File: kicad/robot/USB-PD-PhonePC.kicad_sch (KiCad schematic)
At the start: 40 parts, among them IC1 TPS61253AYFFR, U11 MAX77958EWV+T, U15 ESD122DMYR

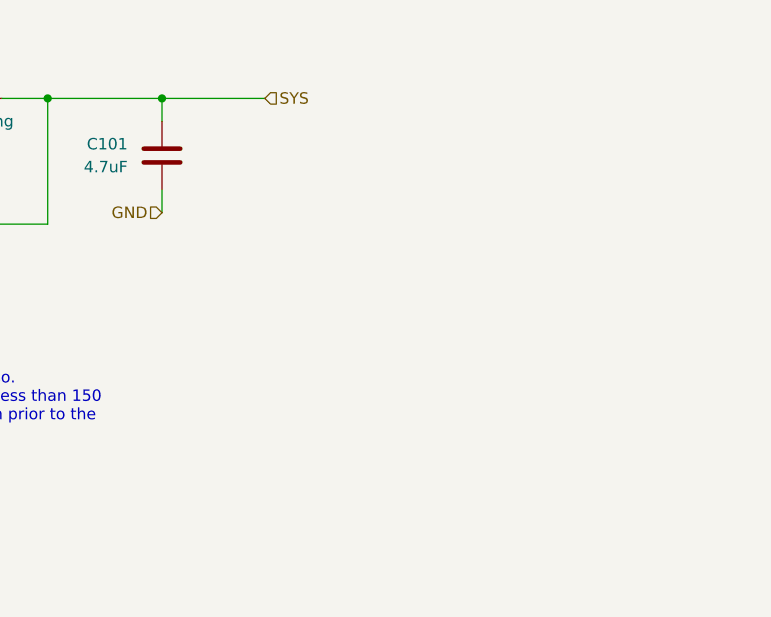
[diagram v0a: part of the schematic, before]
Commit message: Added dual mosfet to MCU PD side as well. To discuss
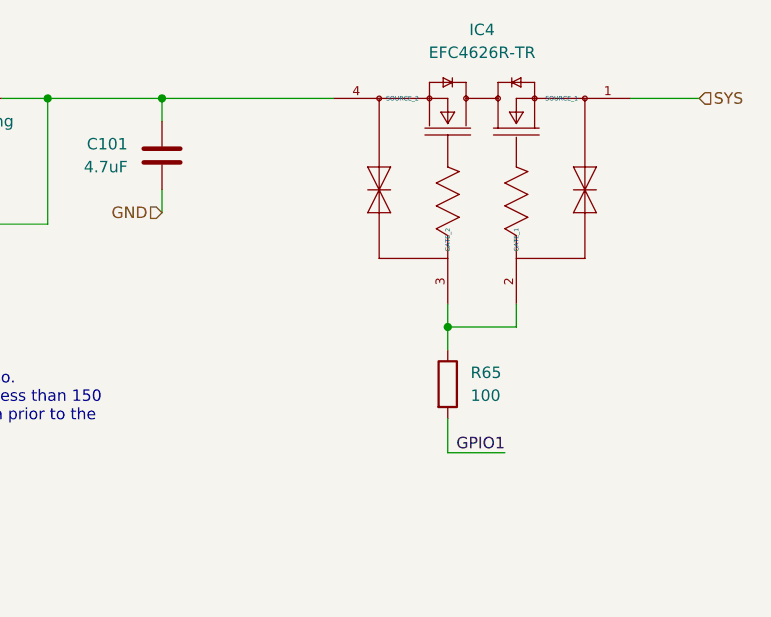
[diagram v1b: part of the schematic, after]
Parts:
- added IC4: EFC4626R-TR, Package_BGA:ON_SEMI_EFCP1010-4DG-020, symbol Power_Management:EFC4626R-TR
- added R65: 100, Resistor_SMD:R_0603_1608Metric, symbol Device:R
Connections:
- net GPIO1: now also R65.2
- net SYS: now also IC4.1 (SOURCE_1); no longer C101.1, IC1.A3 (VIN), L4.1
- new net: IC4.2 (GATE_1), IC4.3 (GATE_2), R65.1
- new net: C101.1, IC1.A3 (VIN), IC4.4 (SOURCE_2), L4.1
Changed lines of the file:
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@@
   (junction (at 231.14 267.97) (diameter 0) (color 0 0 0 0)
   )
+  (junction (at 317.5 220.98) (diameter 0) (color 0 0 0 0)
+  )
+  (junction (at 213.36 175.26) (diameter 0) (color 0 0 0 0)
+  )
   (junction (at 422.91 130.81) (diameter 0) (color 0 0 0 0)
   )
-  (junction (at 317.5 220.98) (diameter 0) (color 0 0 0 0)
-  )
-  (junction (at 213.36 175.26) (diameter 0) (color 0 0 0 0)
-  )
   (junction (at 248.92 130.81) (diameter 0) (color 0 0 0 0)
   )
@@
   )
   (junction (at 331.47 246.38) (diameter 0) (color 0 0 0 0)
+  )
+  (junction (at 454.66 156.21) (diameter 0) (color 0 0 0 0)
   )
   (junction (at 339.09 234.95) (diameter 0) (color 0 0 0 0)
@@
     (stroke (width 0) (type default) (color 0 0 0 0))
   )
+  (wire (pts (xy 454.66 166.37) (xy 454.66 170.18))
+    (stroke (width 0) (type default) (color 0 0 0 0))
+  )
   (wire (pts (xy 410.21 130.81) (xy 422.91 130.81))
     (stroke (width 0) (type default) (color 0 0 0 0))
@@
     (stroke (width 0) (type default) (color 0 0 0 0))
   )
+  (wire (pts (xy 454.66 170.18) (xy 461.01 170.18))
+    (stroke (width 0) (type default) (color 0 0 0 0))
+  )
   (wire (pts (xy 321.31 203.2) (xy 321.31 191.77))
     (stroke (width 0) (type default) (color 0 0 0 0))
@@
     (stroke (width 0) (type default) (color 0 0 0 0))
   )
+  (wire (pts (xy 462.28 153.67) (xy 462.28 156.21))
+    (stroke (width 0) (type default) (color 0 0 0 0))
+  )
   (wire (pts (xy 227.33 215.9) (xy 264.16 215.9))
     (stroke (width 0) (type default) (color 0 0 0 0))
@@
     (stroke (width 0) (type default) (color 0 0 0 0))
   )
+  (wire (pts (xy 454.66 156.21) (xy 454.66 153.67))
+    (stroke (width 0) (type default) (color 0 0 0 0))
+  )
   (wire (pts (xy 309.88 259.08) (xy 316.23 259.08))
     (stroke (width 0) (type default) (color 0 0 0 0))
@@
     (stroke (width 0) (type default) (color 0 0 0 0))
   )
+  (wire (pts (xy 422.91 130.81) (xy 441.96 130.81))
+    (stroke (width 0) (type default) (color 0 0 0 0))
+  )
   (wire (pts (xy 248.92 198.12) (xy 248.92 130.81))
     (stroke (width 0) (type default) (color 0 0 0 0))
@@
     (stroke (width 0) (type default) (color 0 0 0 0))
   )
+  (wire (pts (xy 454.66 158.75) (xy 454.66 156.21))
+    (stroke (width 0) (type default) (color 0 0 0 0))
+  )
   (wire (pts (xy 339.09 269.24) (xy 339.09 264.16))
     (stroke (width 0) (type default) (color 0 0 0 0))
@@
     (stroke (width 0) (type default) (color 0 0 0 0))
   )
+  (wire (pts (xy 462.28 156.21) (xy 454.66 156.21))
+    (stroke (width 0) (type default) (color 0 0 0 0))
+  )
+  (wire (pts (xy 474.98 130.81) (xy 482.6 130.81))
+    (stroke (width 0) (type default) (color 0 0 0 0))
+  )
   (wire (pts (xy 309.88 218.44) (xy 317.5 218.44))
     (stroke (width 0) (type default) (color 0 0 0 0))
@@
   )
   (wire (pts (xy 335.28 142.24) (xy 335.28 144.78))
-    (stroke (width 0) (type default) (color 0 0 0 0))
-  )
-  (wire (pts (xy 422.91 130.81) (xy 434.34 130.81))
     (stroke (width 0) (type default) (color 0 0 0 0))
   )
@@
     (effects (font (size 1.27 1.27)) (justify right bottom))
   )
+  (label "GPIO1" (at 461.01 170.18 180)
+    (effects (font (size 1.27 1.27)) (justify right bottom))
+  )
   (label "GPIO0" (at 330.2 280.67 0)
     (effects (font (size 1.27 1.27)) (justify left bottom))
@@
     (effects (font (size 1.27 1.27)) (justify left))
   )
-  (hierarchical_label "SYS" (shape input) (at 434.34 130.81 0)
+  (hierarchical_label "SYS" (shape input) (at 482.6 130.81 0)
     (effects (font (size 1.27 1.27)) (justify left))
   )
@@
     (pin "1")
     (pin "2")
+  )
+  (symbol (lib_id "Power_Management:EFC4626R-TR") (at 458.47 140.97 90) (unit 1)
+    (in_bom yes) (on_board yes) (fields_autoplaced)
+    (property "Reference" "IC4" (id 0) (at 458.47 123.19 90))
+    (property "Value" "EFC4626R-TR" (id 1) (at 458.47 125.73 90))
+    (property "Footprint" "Package_BGA:ON_SEMI_EFCP1010-4DG-020" (id 2) (at 415.925 150.495 0)
+      (effects (font (size 1.27 1.27)) (justify left) hide)
+    )
+    (property "Datasheet" "http://www.onsemi.com/pub/Collateral/ENA2292-D.PDF" (id 3) (at 418.465 150.495 0)
+      (effects (font (size 1.27 1.27)) (justify left) hide)
+    )
+    (property "Description" "MOSFET NCH+NCH 2.5V DRIVE" (id 4) (at 421.005 150.495 0)
+      (effects (font (size 1.27 1.27)) (justify left) hide)
+    )
+    (property "Height" "0.22" (id 5) (at 423.545 150.495 0)
+      (effects (font (size 1.27 1.27)) (justify left) hide)
+    )
+    (property "Manufacturer_Name" "onsemi" (id 6) (at 426.085 150.495 0)
+      (effects (font (size 1.27 1.27)) (justify left) hide)
+    )
+    (property "Manufacturer_Part_Number" "EFC4626R-TR" (id 7) (at 428.625 150.495 0)
+      (effects (font (size 1.27 1.27)) (justify left) hide)
+    )
+    (property "Mouser Part Number" "863-EFC4626R-TR" (id 8) (at 431.165 150.495 0)
+      (effects (font (size 1.27 1.27)) (justify left) hide)
+    )
+    (property "Mouser Price/Stock" "https://www.mouser.com/Search/Refine.aspx?Keyword=863-EFC4626R-TR" (id 9) (at 433.705 150.495 0)
+      (effects (font (size 1.27 1.27)) (justify left) hide)
+    )
+    (property "Arrow Part Number" "" (id 10) (at 436.245 150.495 0)
+      (effects (font (size 1.27 1.27)) (justify left) hide)
+    )
+    (property "Arrow Price/Stock" "" (id 11) (at 438.785 150.495 0)
+      (effects (font (size 1.27 1.27)) (justify left) hide)
+    )
+    (property "Mouser Testing Part Number" "" (id 12) (at 441.325 150.495 0)
+      (effects (font (size 1.27 1.27)) (justify left) hide)
+    )
+    (property "Mouser Testing Price/Stock" "" (id 13) (at 483.87 109.22 0)
+      (effects (font (size 1.27 1.27)) (justify left) hide)
+    )
+    (pin "1")
+    (pin "2")
+    (pin "3")
+    (pin "4")
   )
   (symbol (lib_id "Device:C") (at 231.14 259.08 0) (unit 1)
@@
       (effects (font (size 1.27 1.27)) hide)
     )
+    (pin "1")
+    (pin "2")
+  )
+  (symbol (lib_id "Device:R") (at 454.66 162.56 0) (unit 1)
+    (in_bom yes) (on_board yes) (fields_autoplaced)
+    (property "Reference" "R65" (id 0) (at 457.2 161.2899 0)
+      (effects (font (size 1.27 1.27)) (justify left))
+    )
+    (property "Value" "100" (id 1) (at 457.2 163.8299 0)
+      (effects (font (size 1.27 1.27)) (justify left))
+    )
+    (property "Footprint" "Resistor_SMD:R_0603_1608Metric" (id 2) (at 452.882 162.56 90)
+      (effects (font (size 1.27 1.27)) hide)
+    )
+    (property "Datasheet" "~" (id 3) (at 454.66 162.56 0)
+      (effects (font (size 1.27 1.27)) hide)
+    )

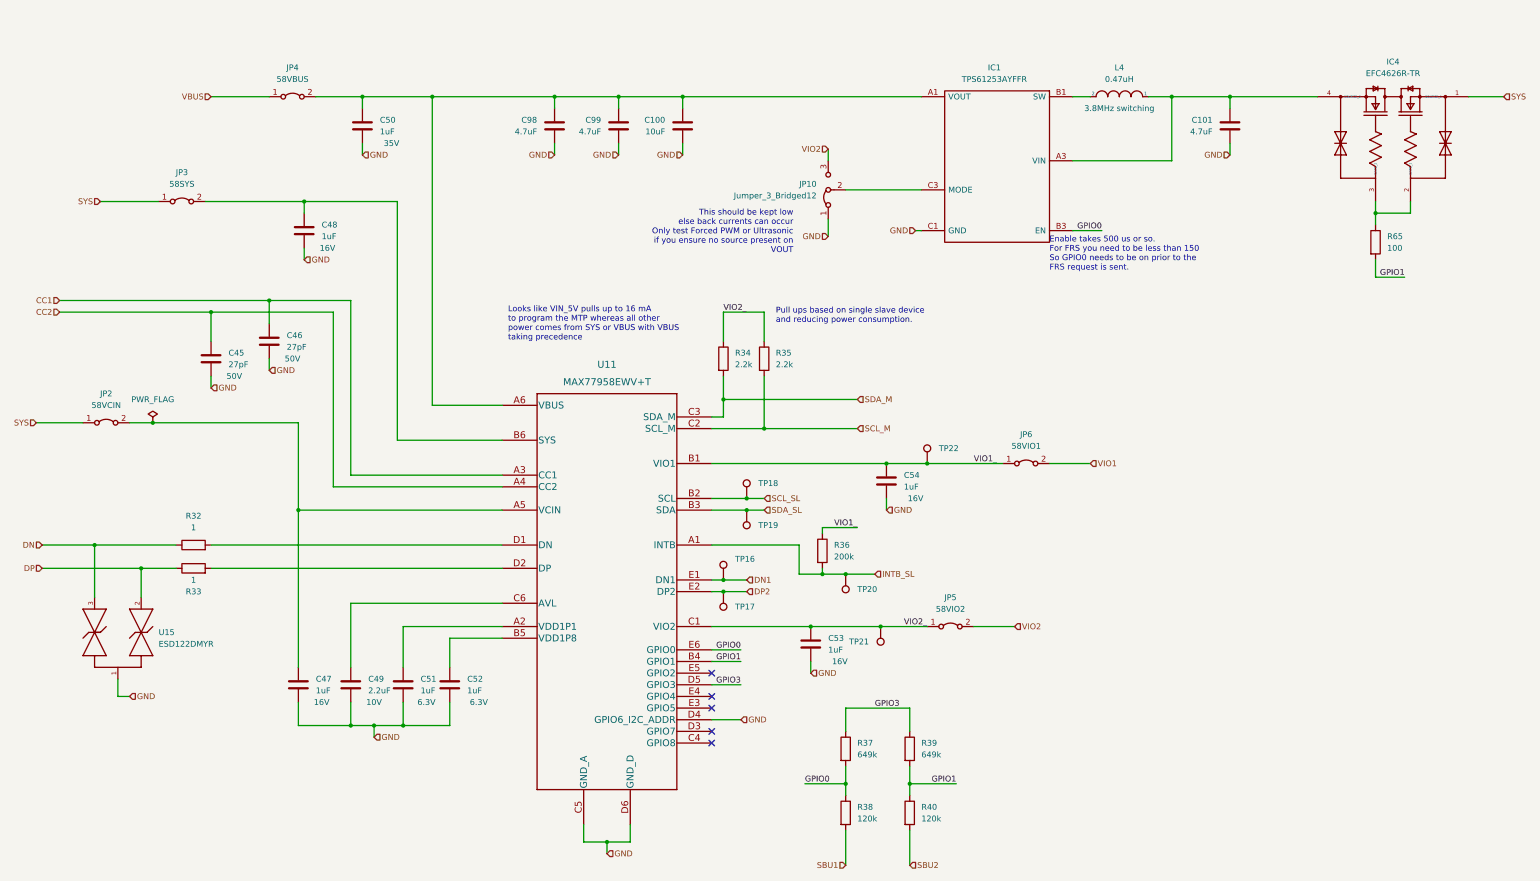
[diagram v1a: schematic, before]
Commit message: Cosmetic rework of USB-PD-PhonePC
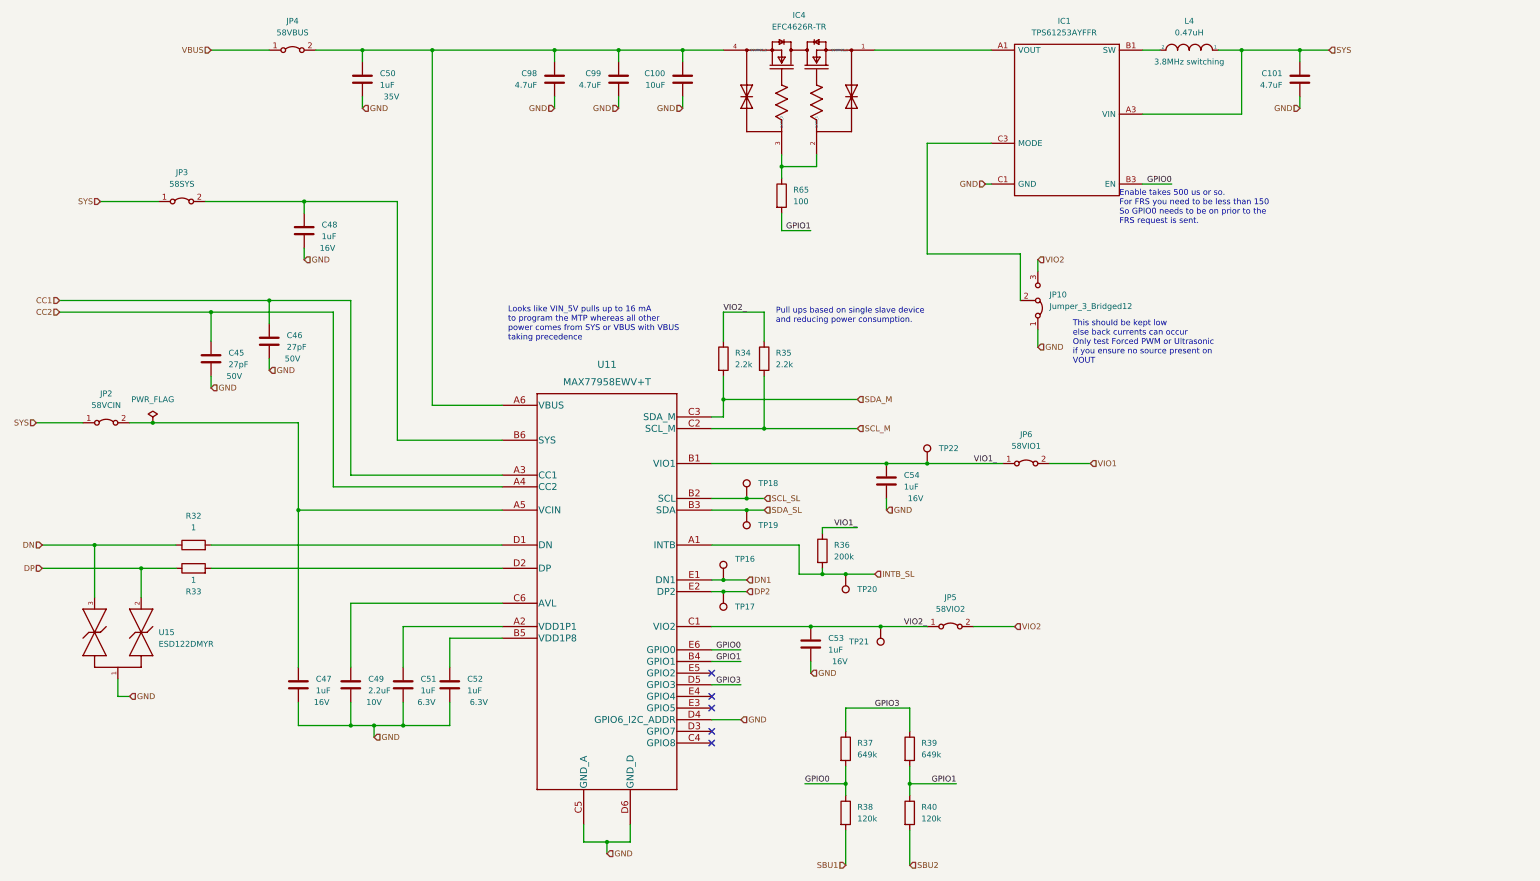
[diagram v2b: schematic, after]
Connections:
- net SYS: now also C101.1, IC1.A3 (VIN), L4.1; no longer IC4.1 (SOURCE_1)
- net at C100.1, C50.1, C98.1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: now also IC4.4 (SOURCE_2); no longer IC1.A1 (VOUT), IC1.A2 (VOUT)
- new net: IC1.A1 (VOUT), IC1.A2 (VOUT), IC4.1 (SOURCE_1)
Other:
- moved on the sheet: C100, C101, C50, C98, C99, IC1, IC4, JP10, JP4, L4, R65

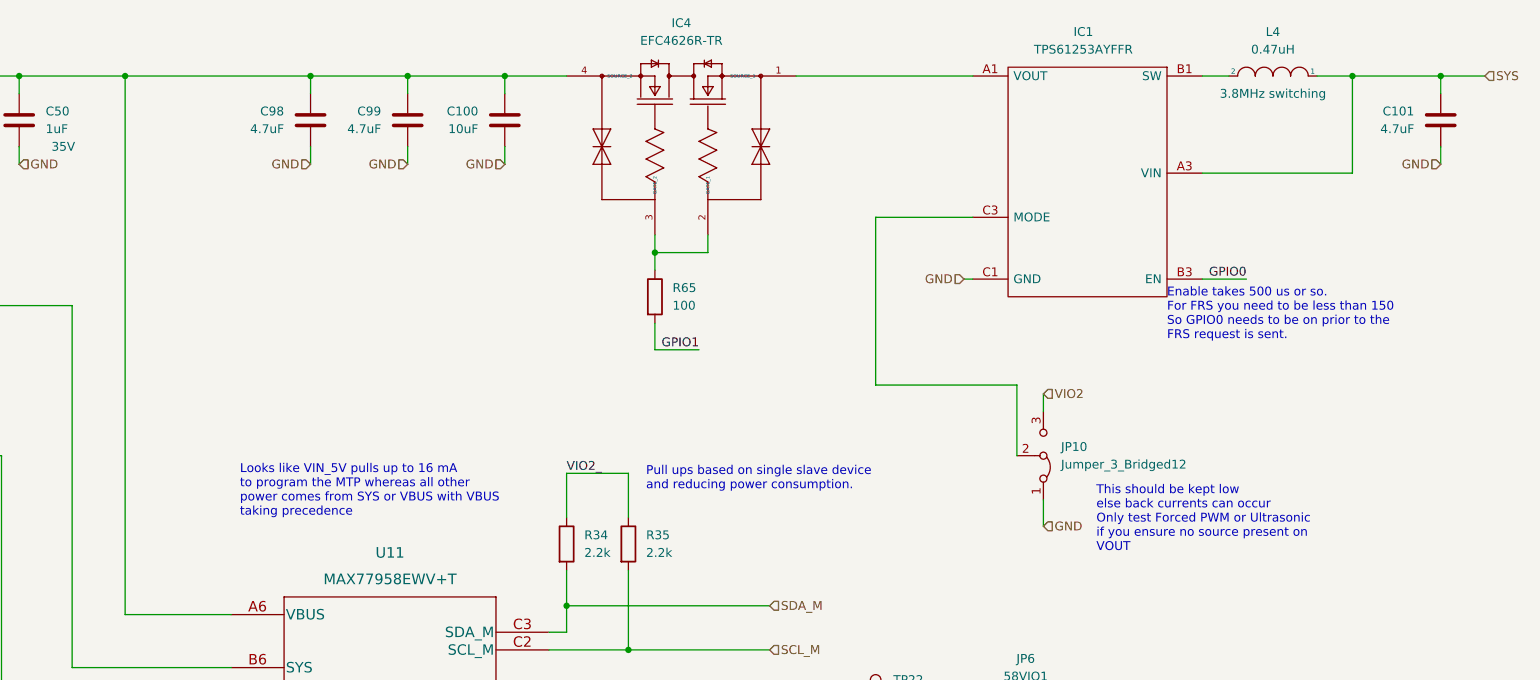
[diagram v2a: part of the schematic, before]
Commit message: Moved caps closer to boost reg in PD sheet
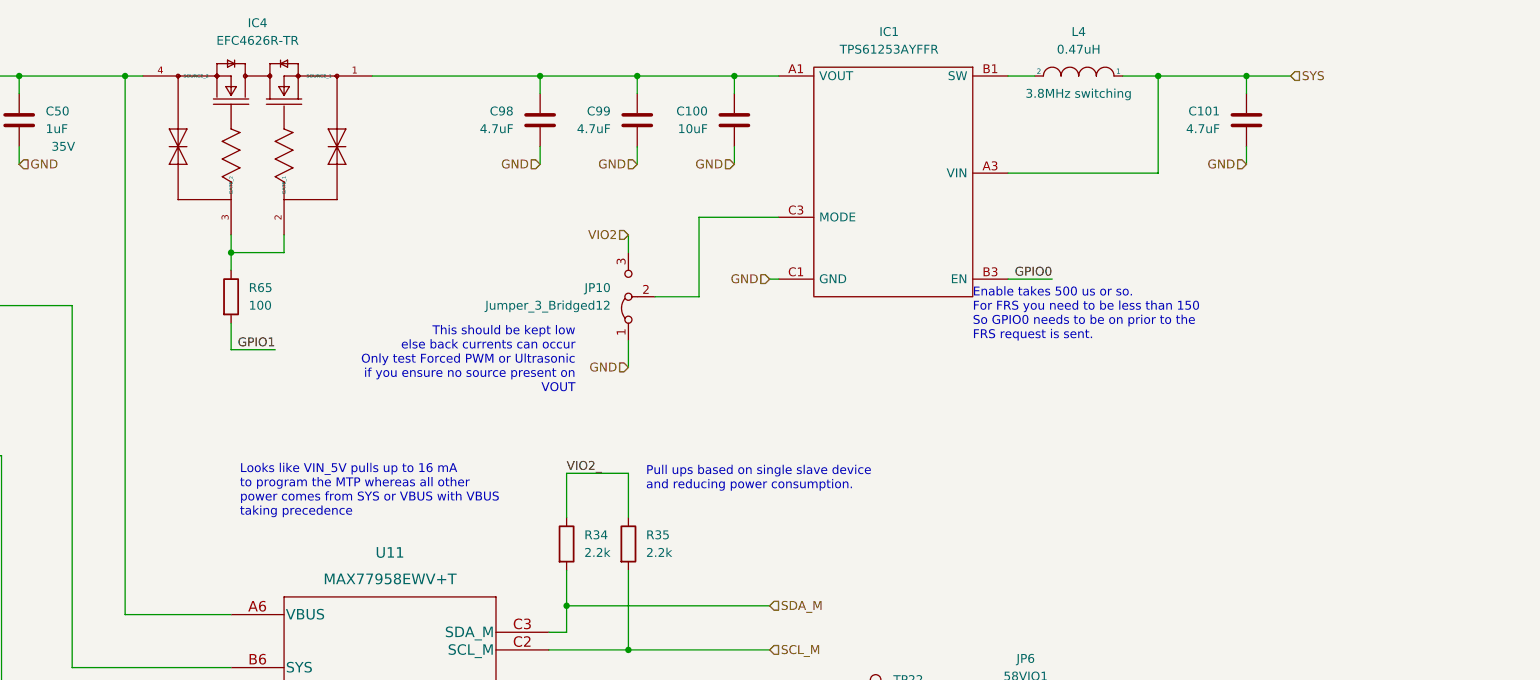
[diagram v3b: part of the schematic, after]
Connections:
- net at IC1.A1 (VOUT), IC1.A2 (VOUT), IC4.1 (SOURCE_1): now also C100.1, C98.1, C99.1
- net at C50.1, IC4.4 (SOURCE_2), JP4.2 (B)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: no longer C100.1, C98.1, C99.1
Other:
- moved on the sheet: C100, C101, C98, C99, IC1, IC4, JP10, L4, R65
